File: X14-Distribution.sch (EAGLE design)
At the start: 0 parts

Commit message: Added the Reverse voltage blocker from the tether, OR MOSFET controller, and ON/OFF signal for Bricks
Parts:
- added C1: 330uF, CAP, aluminin-capacitor-brick-UCM1H331MNL1GS:UCM1H331MNL1GS
- added D1, D10, D9: 15V, SparkFun-DiscreteSemi:DIODE-ZENER-BZT52C3V6S
- added D2, D3: 19V, SparkFun-DiscreteSemi:DIODE-ZENER-BZT52C3V6S
- added D4, D5: 250mA/100V, SparkFun-DiscreteSemi:DIODE-BAS16J
- added D6: 5V, SparkFun-DiscreteSemi:DIODE-ZENER-BZT52C3V6S
- added D7, D8: (no value), SparkFun-LED:LED0603
- added JP1: JUMPER-SMT_2_NO_SILK, SparkFun-Jumpers:JUMPER-SMT_2_NO_SILK
- added Q1, Q5, Q6, Q7, Q8: 310mA/60V/1.6Ω, SparkFun-DiscreteSemi:MOSFET-NCH-2N7002PW
- added Q2, Q3, Q4: IRF1018EPBF, TRANS, Dist_Reverse_Voltage_NMOS:IRF1018EPBF
- added R1, R2: 1M, SparkFun-Resistors:RESISTOR0603
- added R3, R6, R7, R8, R9: 10k, SparkFun-Resistors:RESISTOR0603
- added R4, R5: 470, SparkFun-Resistors:RESISTOR0603
- added U1, U2: DIST_OR_CONTROL_ALTMK06A-M, IC, Dist_OR_Controller:DIST_OR_CONTROL_ALTMK06A-M
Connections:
- new net +12V: C1.+, D7.A, D8.A, Q3.D, U1.OUT, U1.VS, U2.VS
- new net +12V_B: Q4.S, U2.IN
- new net +12_A: Q3.S, U1.IN
- new net +48V: D3.C, D5.C, Q5.D, Q6.D, R1.2, R3.2
- new net 12V_GND: C1.-, Q7.S, Q8.S, R6.1, R7.1, R8.1, R9.1, U1.GND, U2.GND
- new net 48V_GND: D1.A, D6.A, JP1.1, Q1.S, Q2.S, R2.1
- new net GND_RAW: Q2.D
- new net N$1: D1.C, Q2.G, R1.1
- new net N$10: Q4.D, U2.OUT
- new net N$11: D10.C, Q6.S, R8.2
- new net N$12: D10.A, Q8.G, R9.2
- new net N$13: D7.C, R4.2
- new net N$14: Q8.D, R5.1
- new net N$15: D8.C, R5.2
- new net N$2: D4.C, D5.A, Q1.G
- new net N$4: D2.C, D3.A
- new net N$5: D9.C, Q5.S, R6.2
- new net N$6: D2.A, D4.A, R2.2
- new net N$7: D9.A, Q7.G, R7.2
- new net N$9: Q7.D, R4.1
- new net ON/OFF: D6.C, JP1.2, Q1.D, R3.1
- new net OR_DRIVE_A: Q3.G, Q5.G, U1.GATE
- new net OR_DRIVE_B: Q4.G, Q6.G, U2.GATE

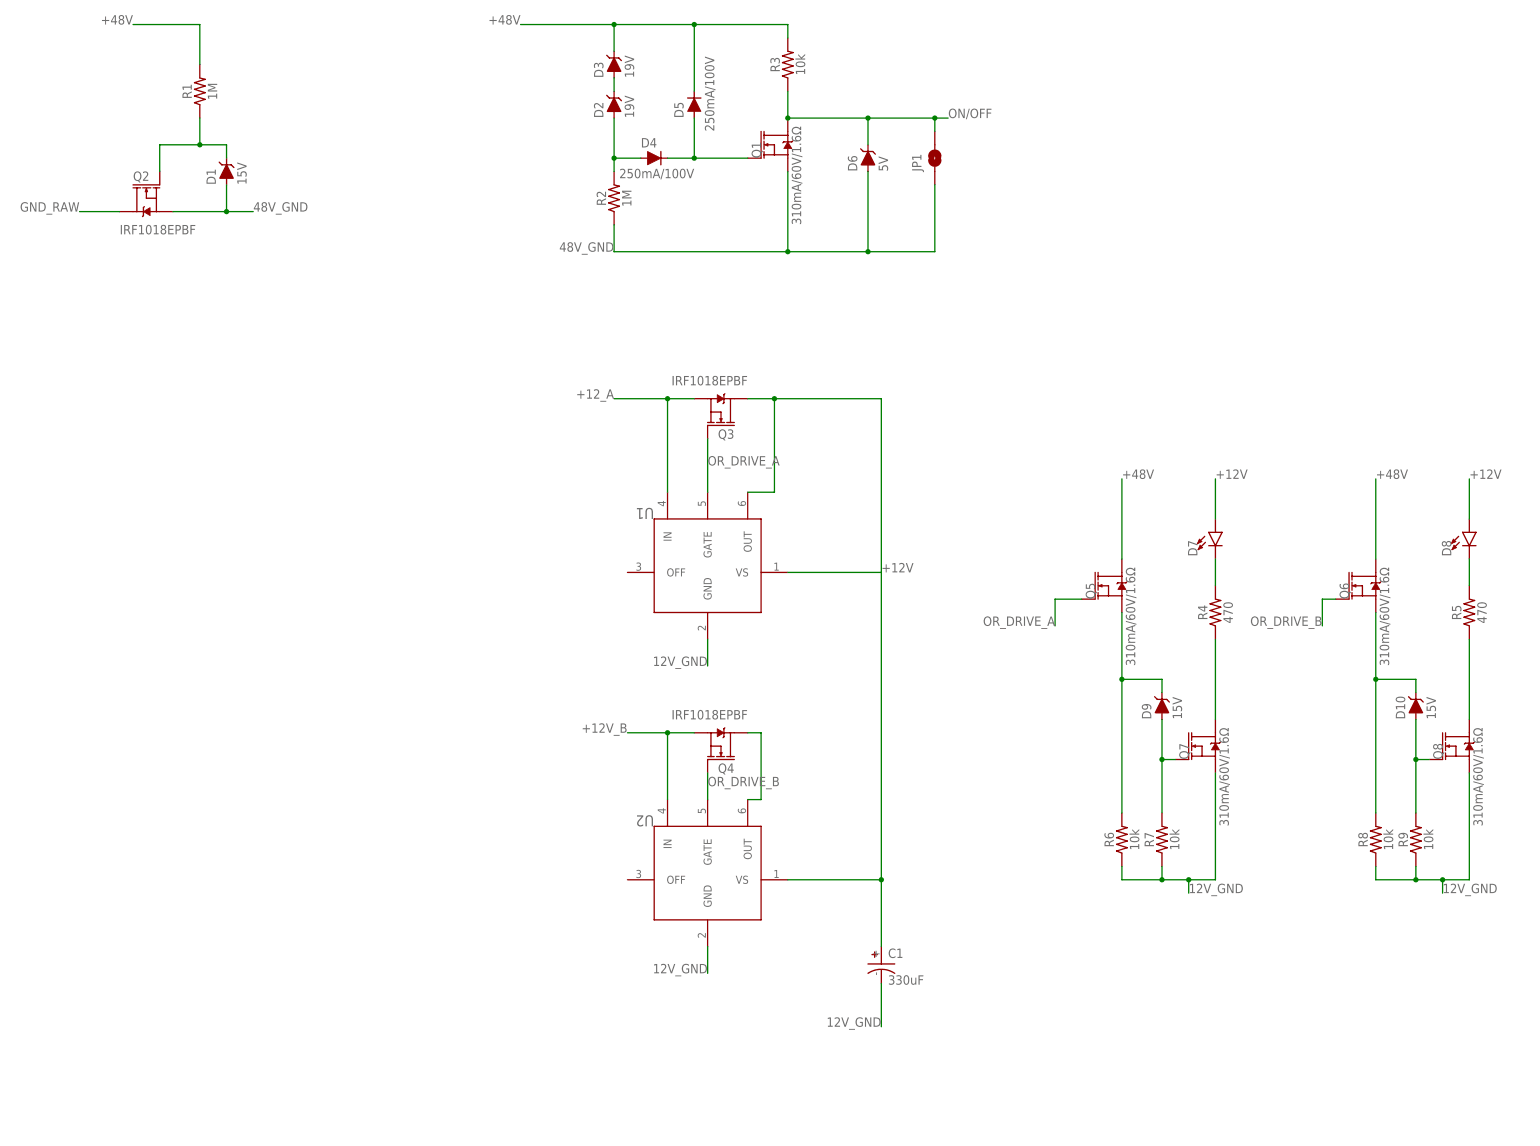
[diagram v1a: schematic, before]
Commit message: Added the schottky diode ORing for the conversion board
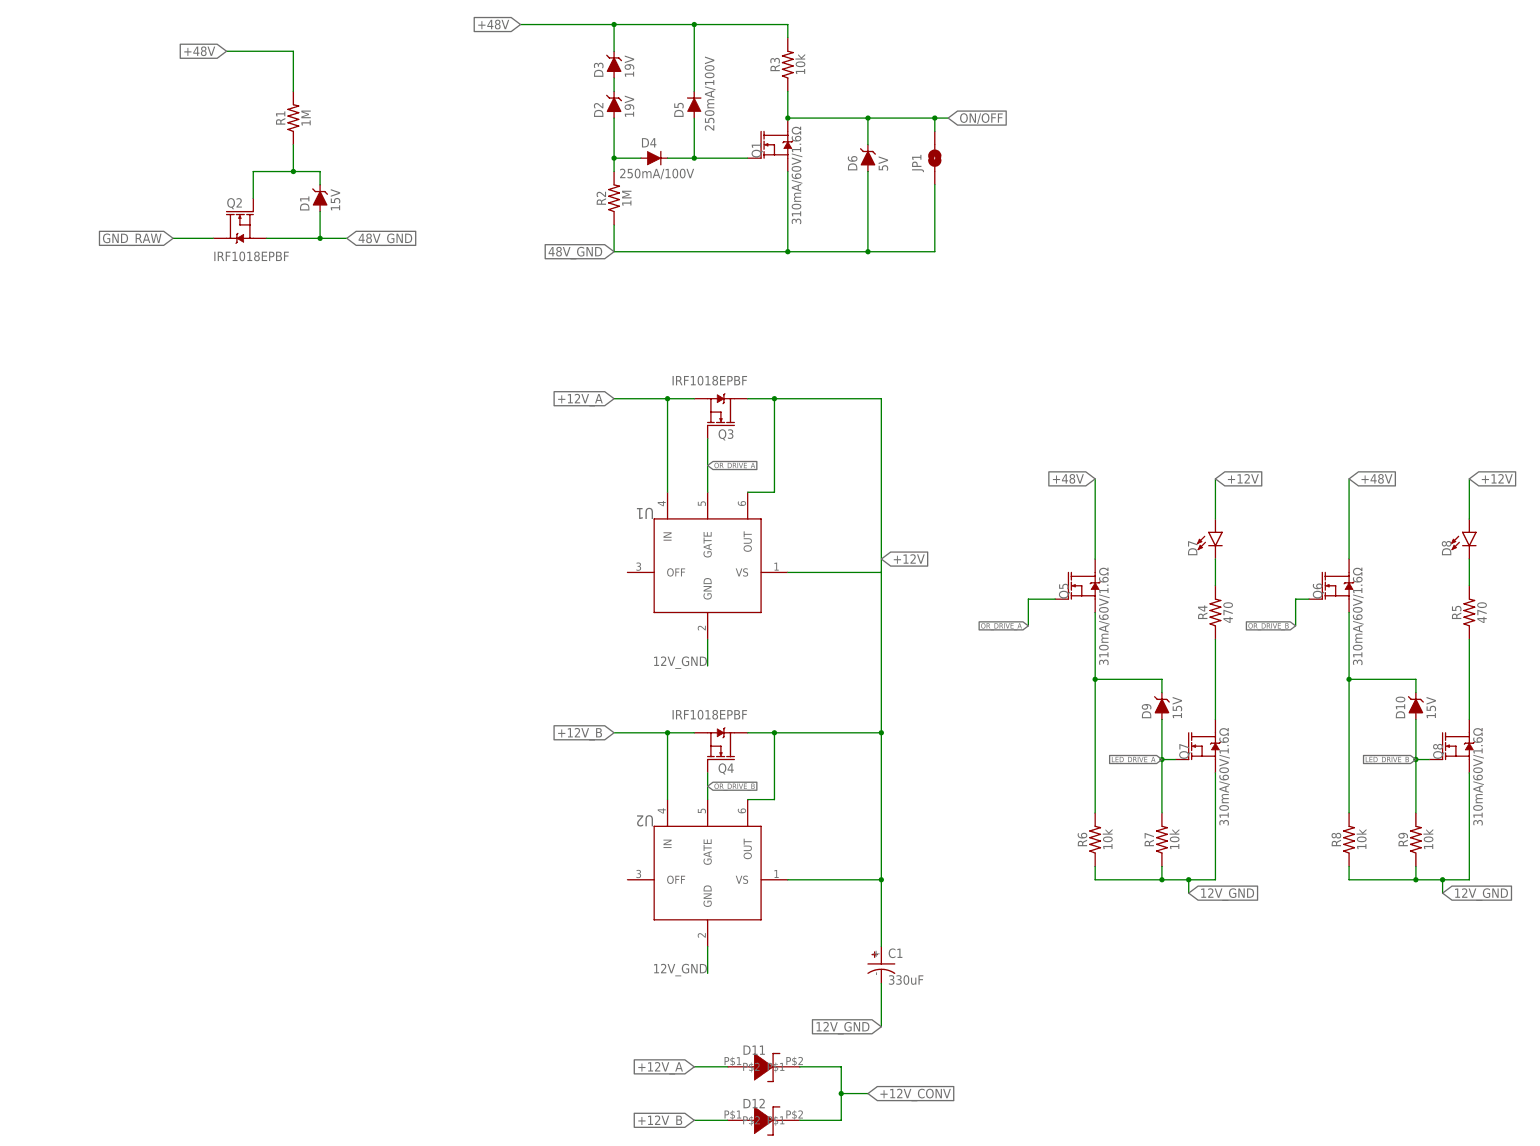
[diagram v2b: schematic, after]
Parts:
- added D11, D12: DIODE-DO-214AC(SK34ATR), DISTRIBUTION, Oring Schottky Diode:DIODE-DO-214AC(SK34ATR)
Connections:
- net N$12 renamed LED_DRIVE_B
- net N$7 renamed LED_DRIVE_A
- removed net +12_A: Q3.S, U1.IN
- removed net N$10: Q4.D, U2.OUT
- new net +12V_A: D11.P$1, Q3.S, U1.IN
- new net +12V_CONV: D11.P$2, D12.P$2
- net +12V: now also Q4.D, U2.OUT
- net +12V_B: now also D12.P$1
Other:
- moved on the sheet: D1, Q2, Q5, Q6, R1, R6, R8

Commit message: Added the test points, points of entry for different voltage levels, and power connection to the Backplane
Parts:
- added 12GND_TEST, 12V_A_TEST, 12V_B_TEST, 12V_TEST, 48GND_TEST, 48V_TEST, ON/OFF_TEST: (no value), SparkFun-Connectors:CONN_01
- added 48V_POE, 5V_POE: POE_TERMINAL, CONN, 2 pin screw terminal:POE_TERMINAL
- added BACKPLANE_POWER: (no value), CONN, Samtec MPPT Hermaphoditic 10 pos - MPPT-10-01-01-L-RA-SD:MPPT-10-01-01-L-RA-SD
- added DATA_TEST: (no value), SparkFun-Connectors:CONN_02
- added H1, H2, H3, H4: 6-32-HOLE, OTHER, Mounting Holes:6-32-HOLE
- added TETHER: DIST_TO_TETHER, CONN, 6 pin connector to screw connector:DIST_TO_TETHER
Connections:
- new net +5V: 5V_POE.2
- new net 5V_GND: 5V_POE.1
- new net CLK: DATA_TEST.1
- new net DATA: DATA_TEST.2
- net +12V: now also 12V_TEST.1, BACKPLANE_POWER.1, BACKPLANE_POWER.2, BACKPLANE_POWER.3, BACKPLANE_POWER.4, BACKPLANE_POWER.5
- net +12V_A: now also 12V_A_TEST.1
- net +12V_B: now also 12V_B_TEST.1
- net +48V: now also 48V_POE.2, 48V_TEST.1, TETHER.4, TETHER.5, TETHER.6
- net 12V_GND: now also 12GND_TEST.1, BACKPLANE_POWER.10, BACKPLANE_POWER.6, BACKPLANE_POWER.7, BACKPLANE_POWER.8, BACKPLANE_POWER.9
- net 48V_GND: now also 48GND_TEST.1, 48V_POE.1
- net GND_RAW: now also TETHER.1, TETHER.2, TETHER.3
- net ON/OFF: now also ON/OFF_TEST.1

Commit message: Added conversion board connector
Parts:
- added CONVERSION: DISTRIBUTION-CONVERSION, CONN, Distribution-Conversion:DISTRIBUTION-CONVERSION
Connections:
- new net +3.3V: CONVERSION.VOUT+_3
- net +12V_CONV: now also CONVERSION.VIN+
- net +5V: now also CONVERSION.VOUT+_5
- net 12V_GND: now also CONVERSION.VIN-
- net 5V_GND: now also CONVERSION.VOUT-
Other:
- moved on the sheet: 12GND_TEST, 12V_A_TEST, 12V_B_TEST, 12V_TEST, 48GND_TEST, 48V_POE, 48V_TEST, 5V_POE, BACKPLANE_POWER, C1, D1, D10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

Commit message: Added descriptive green text and some connectors
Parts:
- added BACKPLANE: DISTRIBUTION-BACKPLANE, CONN, Distribution-Backplane:DISTRIBUTION-BACKPLANE
- added R10, R11, R12, R13: 10k, SparkFun-Resistors:RESISTOR0603
- D11, D12: device DISTRIBUTION, Oring Schottky Diode:DIODE-DO-214AC(SK34ATR) -> DIODE, Oring Schottky Diode:DIODE-DO-214AC(SK34ATR)
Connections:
- new net ALERT_1: BACKPLANE.ALERT_1, R11.1
- new net ALERT_2: BACKPLANE.ALERT_2, R12.1
- new net C2_1: BACKPLANE.C2_1
- new net C2_2: BACKPLANE.C2_2
- net +12V_A: now also D11.1; no longer D11.P$1
- net +12V_B: now also D12.1; no longer D12.P$1
- net +12V_CONV: now also D11.2, D12.2; no longer D11.P$2, D12.P$2
- net +3.3V: now also BACKPLANE.3.3V, R10.2, R11.2, R12.2, R13.2
- net +5V: now also BACKPLANE.5V
- net 5V_GND: now also BACKPLANE.GND_5V
- net CLK: now also BACKPLANE.CLK, R13.1
- net DATA: now also BACKPLANE.DATA, R10.1
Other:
- note added: "BACKPLANE CONNECTORS"
- note added: "LATCH THAT KEEPS ON/OFF LOW AFTER IT FIRST GOES LOW"
- note added: "OR MOSFET CONTROLLERS"
- note added: "OR MOSFET INDICATOR LEDS"
- note added: "ORING DIODES TO CONVERSION"
- note added: "REVERSE VOLTAGE PROTECTION"
- note added: "TURN ON/OFF CIRCUIT"
- moved on the sheet: 12GND_TEST, 12V_A_TEST, 12V_B_TEST, 12V_TEST, 48GND_TEST, 48V_POE, 48V_TEST, 5V_POE, BACKPLANE_POWER, C1, CONVERSION, D1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

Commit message: Added connectors to Bricks and some more extra green explanation text
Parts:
- added BRICKS1, BRICKS2: PETC-02-40-02-01-X-VT(DTOB), CONN_Distribution-Bricks:PETC-02-40-02-01-X-VT(DTOB)
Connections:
- net +12V_A: now also BRICKS1.12V
- net +12V_B: now also BRICKS2.12V
- net +48V: now also BRICKS1.48V, BRICKS2.48V
- net 12V_GND: now also BRICKS1.12VGND, BRICKS2.12VGND
- net 48V_GND: now also BRICKS1.48VGND, BRICKS2.48VGND
- net ALERT_1: now also BRICKS1.ALERT
- net ALERT_2: now also BRICKS2.ALERT
- net C2_1: now also BRICKS1.C2
- net C2_2: now also BRICKS2.C2
- net CLK: now also BRICKS1.CLK, BRICKS2.CLK
- net DATA: now also BRICKS1.DATA, BRICKS2.DATA
- net ON/OFF: now also BRICKS1.ON/OFF, BRICKS2.ON/OFF
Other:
- note added: "BRICKS CONNECTORS"
- note added: "CONNECTOR TO CONVERSION BOARD"
- note added: "Points of Entry for different voltages"
- note added: "TESTING POINTS '"
- moved on the sheet: 48GND_TEST, 48V_POE, 48V_TEST, 5V_POE, BACKPLANE, CONVERSION, D10, D7, D8, D9, DATA_TEST, ON/OFF_TEST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

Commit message: Added more green explanatory text, and spread out the schematic to make it look better
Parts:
- removed CONVERSION: DISTRIBUTION-CONVERSION, CONN, Distribution-Conversion:DISTRIBUTION-CONVERSION
- added U$1: DISTRIBUTION-CONVERSION, CONN, Distribution-Conversion:DISTRIBUTION-CONVERSION
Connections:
- net +12V: now also U$1.VIN+
- net +12V_CONV: no longer CONVERSION.VIN+
- net +3.3V: now also U$1.VOUT+_3; no longer CONVERSION.VOUT+_3
- net +5V: now also U$1.VOUT+_5; no longer CONVERSION.VOUT+_5
- net 12V_GND: now also U$1.VIN-; no longer CONVERSION.VIN-
- net 5V_GND: now also U$1.VOUT-; no longer CONVERSION.VOUT-
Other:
- note added: "(to make sure the tether isn't plugged in the wrong way)"
- note added: "Backplane logic connector"
- note added: "Backplane power connector"
- note added: "CONNECTIONS TO BRICKS"
- note added: "CONNECTIONS TO CONVERSION BOARD"
- note added: "CONNECTIONS TO THE BACKPLANE"
- note added: "CONNECTIONS TO THE TETHER"
- note added: "Connector to conversion Board"
- note added: "Data testing points"
- note added: "Latch that keeps ON/OFF low after it first goes low"
- note added: "MISC. CONNECTION POINTS"
- note added: "MISCELLANEOUS CIRCUITS"
- note added: "ORing diodes to conversion"
- note added: "Point of entry for Tether"
- note added: "Reverse voltage protection"
- note added: "Voltage testing points"
- note removed: "BACKPLANE CONNECTORS"
- note removed: "CONNECTOR TO CONVERSION BOARD"
- note removed: "LATCH THAT KEEPS ON/OFF LOW AFTER IT FIRST GOES LOW"
- note removed: "ORING DIODES TO CONVERSION"
- note removed: "REVERSE VOLTAGE PROTECTION"
- note removed: "TESTING POINTS '"
- moved on the sheet: 12GND_TEST, 12V_A_TEST, 12V_B_TEST, 12V_TEST, 48GND_TEST, 48V_POE, 48V_TEST, 5V_POE, BACKPLANE, BACKPLANE_POWER, BRICKS1, BRICKS2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
